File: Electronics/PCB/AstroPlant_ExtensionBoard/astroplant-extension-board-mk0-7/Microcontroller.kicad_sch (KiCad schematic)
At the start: 15 parts, among them IC1 STM32WB55CCU6, J6 629105136821, U1 USBLC6-2SC6

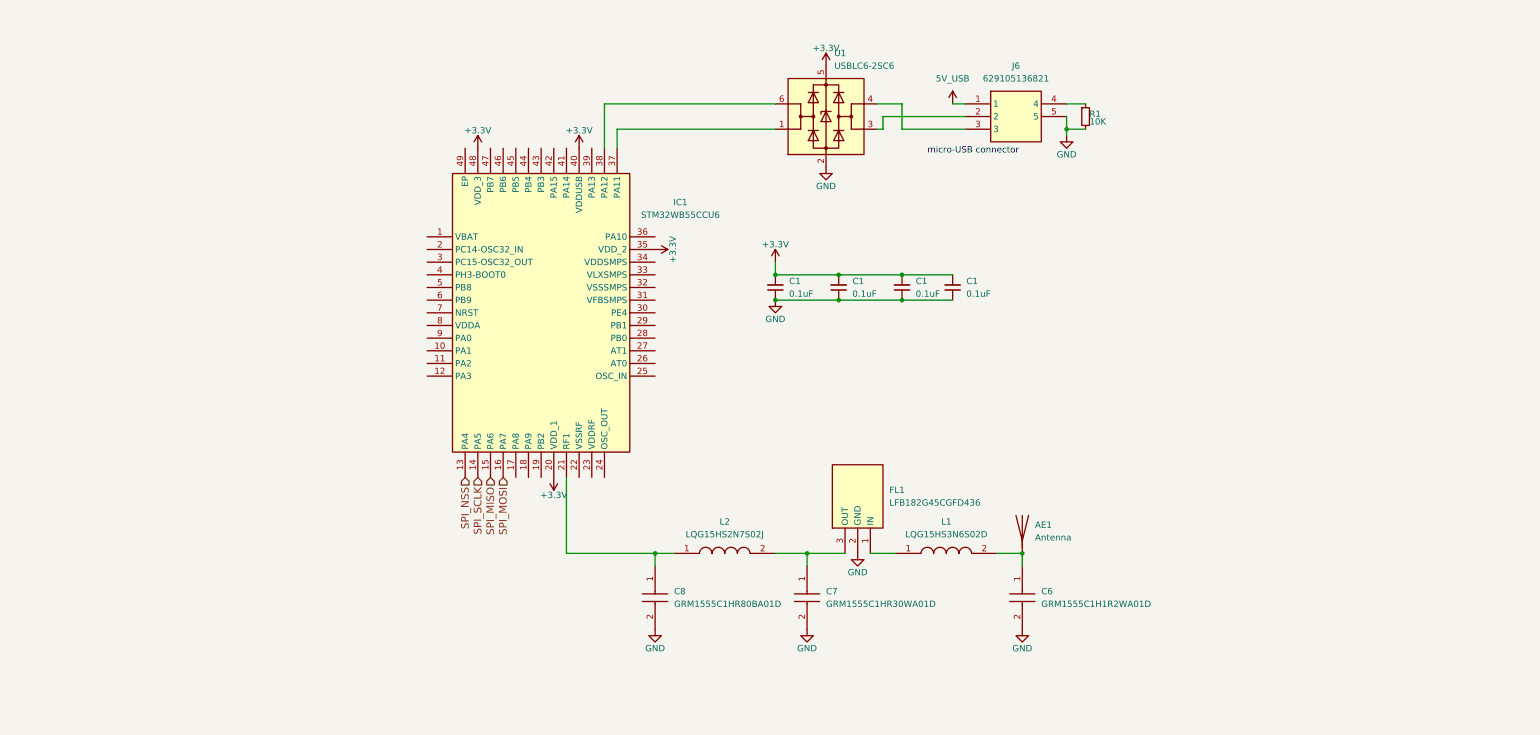
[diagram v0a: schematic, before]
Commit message: Update schematic and change library path
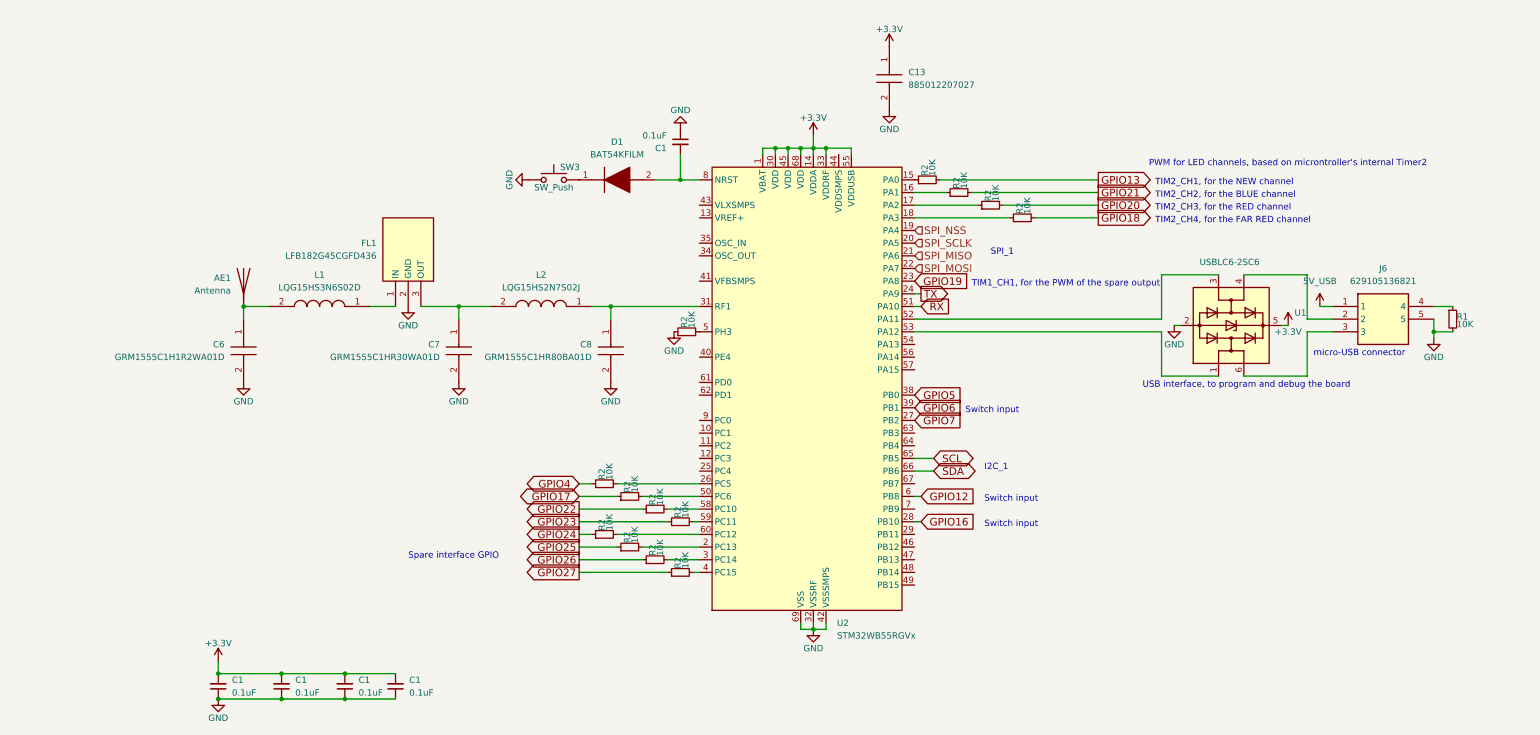
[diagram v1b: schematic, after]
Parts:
- removed IC1: STM32WB55CCU6, QFN50P700X700X60-49N-D, symbol SamacSys_Parts:STM32WB55CCU6
- added C1: 0.1uF, Capacitor_SMD:C_0805_2012Metric, symbol Device:C_Small
- added C13: 885012207027, CAPC2012X90N, symbol SamacSys_Parts:885012207027
- added D1: BAT54KFILM, SODFL1608X70N, symbol SamacSys_Parts:BAT54KFILM
- added R2 (x13): 10K, Resistor_SMD:R_0805_2012Metric, symbol Device:R_Small
- added SW3: SW_Push, Button_Switch_THT:SW_PUSH_6mm, symbol Astroplant_VFR-rescue:SW_Push-Astroplant_VFR-rescue-Astroplant_VFR-rescue
- added U2: STM32WB55RGVx, Package_DFN_QFN:QFN-68-1EP_8x8mm_P0.4mm_EP6.4x6.4mm, symbol MCU_ST_STM32WB:STM32WB55RGVx
- J6: footprint MICRO-USB(2.0-SMT-TYPE-B) -> SamacSys_Parts:MICRO-USB_2.0-SMT-TYPE-B_
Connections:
- net +3V3: now also C13.1, U2.1 (VBAT), U2.14 (VDDA), U2.30 (VDD), U2.33 (VDDRF), U2.45 (VDD), U2.55 (VDDUSB), U2.68 (VDD)
- net GND: now also C1.1, C13.2, R2.1, SW3.1, U2.32 (VSSRF), U2.42 (VSSSMPS), U2.69 (VSS)
- net SPI_MISO: now also U2.21 (PA6)
- net SPI_MOSI: now also U2.22 (PA7)
- net SPI_NSS: now also U2.19 (PA4)
- net SPI_SCLK: now also U2.20 (PA5)
- net at J6.2: now also U1.4 (I/O2); no longer U1.3 (I/O2)
- net at J6.3: now also U1.6 (I/O1); no longer U1.4 (I/O2)
- net at U1.1 (I/O1): now also U2.53 (PA12)
- net at C8.1, L2.1: now also U2.31 (RF1)
- new net: R2.2, U2.5 (PH3)
- new net: R2.2, U2.60 (PC12)
- new net: R2.2, U2.2 (PC13)
- new net: R2.2, U2.4 (PC15)
- new net: R2.1, U2.15 (PA0)
- new net: R2.2, U2.58 (PC10)
- new net: R2.1, U2.18 (PA3)
- new net: U1.3 (I/O2), U2.52 (PA11)
- new net: D1.1, SW3.2
- new net: R2.1, U2.16 (PA1)
- new net: R2.1, U2.17 (PA2)
- new net: R2.2, U2.26 (PC5)
- new net: R2.2, U2.3 (PC14)
- new net: R2.2, U2.50 (PC6)
- new net: R2.2, U2.59 (PC11)
- new net: C1.2, D1.2, U2.8 (NRST)
- new net GPIO12: U2.6 (PB8)
- new net GPIO13: R2.2
- new net GPIO16: U2.28 (PB10)
- new net GPIO17: R2.1
- new net GPIO18: R2.2
- new net GPIO19: U2.23 (PA8)
- new net GPIO20: R2.2
- new net GPIO21: R2.2
- new net GPIO22: R2.1
- new net GPIO23: R2.1
- new net GPIO24: R2.1
- new net GPIO25: R2.1
- new net GPIO26: R2.1
- new net GPIO27: R2.1
- new net GPIO4: R2.1
- new net GPIO5: U2.38 (PB0)
- new net GPIO6: U2.39 (PB1)
- new net GPIO7: U2.27 (PB2)
- new net RX: U2.51 (PA10)
- new net SCL: U2.65 (PB5)
- new net SDA: U2.66 (PB6)
- new net TX: U2.24 (PA9)
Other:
- note added: "I2C_1"
- note added: "PWM for LED channels, based on microntroller's internal Timer2"
- note added: "SPI_1"
- note added: "Spare interface GPIO"
- note added: "Switch input"
- note added: "TIM1_CH1, for the PWM of the spare output"
- note added: "TIM2_CH1, for the NEW channel"
- note added: "TIM2_CH2, for the BLUE channel"
- note added: "TIM2_CH3, for the RED channel"
- note added: "TIM2_CH4, for the FAR RED channel"
- note added: "USB interface, to program and debug the board"
- moved on the sheet: AE1, C1, C6, C7, C8, FL1, J6, L1, L2, R1, U1

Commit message: Place components on PCB
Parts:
- removed C1 (x5): 0.1uF, Capacitor_SMD:C_0805_2012Metric, symbol Device:C_Small
- removed C13: 885012207027, CAPC2012X90N, symbol SamacSys_Parts:885012207027
- removed R1, R2 (x13): 10K, Resistor_SMD:R_0805_2012Metric, symbol Device:R_Small
- added C10, C11, C12, C14, C5, C9: 100nF, Capacitor_SMD:C_0603_1608Metric, symbol Device:C_Small
- added C13: 100pF, Capacitor_SMD:C_0603_1608Metric, symbol Device:C_Small
- added R12, R24: 10k, Resistor_SMD:R_0603_1608Metric, symbol Device:R_Small
- added R13, R14, R15, R16, R17, R18, R19, R20, R21, R22, R23, R6: 1k, Resistor_SMD:R_0603_1608Metric, symbol Device:R_Small
- C6, C7, C8: footprint CAPC1005X55N -> SamacSys_Parts:CAPC1005X55N
- D1: footprint SODFL1608X70N -> SamacSys_Parts:SODFL1608X70N
- FL1: footprint LFB182G45CGFD436 -> SamacSys_Parts:LFB182G45CGFD436
- L1, L2: footprint LQG15WH0N7B02D -> SamacSys_Parts:LQG15WH0N7B02D
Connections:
- net +3V3: now also C10.1, C11.1, C13.1, C14.1, C5.1, C9.1; no longer U2.1 (VBAT)
- net GND: now also C10.2, C11.2, C12.1, C13.2, C14.2, C5.2, C9.2, R12.1, R24.1
- net GPIO13: now also R15.2
- net GPIO17: now also R21.1
- net GPIO18: now also R6.2
- net GPIO20: now also R13.2
- net GPIO21: now also R14.2
- net GPIO22: now also R22.1
- net GPIO23: now also R23.1
- net GPIO24: now also R19.1
- net GPIO25: now also R18.1
- net GPIO26: now also R17.1
- net GPIO27: now also R16.1
- net GPIO4: now also R20.1
- net at J6.4: now also R12.2
- net at U2.5 (PH3): now also R24.2
- net at U2.60 (PC12): now also R19.2
- net at U2.2 (PC13): now also R18.2
- net at U2.4 (PC15): now also R16.2
- net at U2.15 (PA0): now also R15.1
- net at U2.58 (PC10): now also R22.2
- net at U2.18 (PA3): now also R6.1
- net at U2.16 (PA1): now also R14.1
- net at U2.17 (PA2): now also R13.1
- net at U2.26 (PC5): now also R20.2
- net at U2.3 (PC14): now also R17.2
- net at U2.50 (PC6): now also R21.2
- net at U2.59 (PC11): now also R23.2
- net at D1.2, U2.8 (NRST): now also C12.2

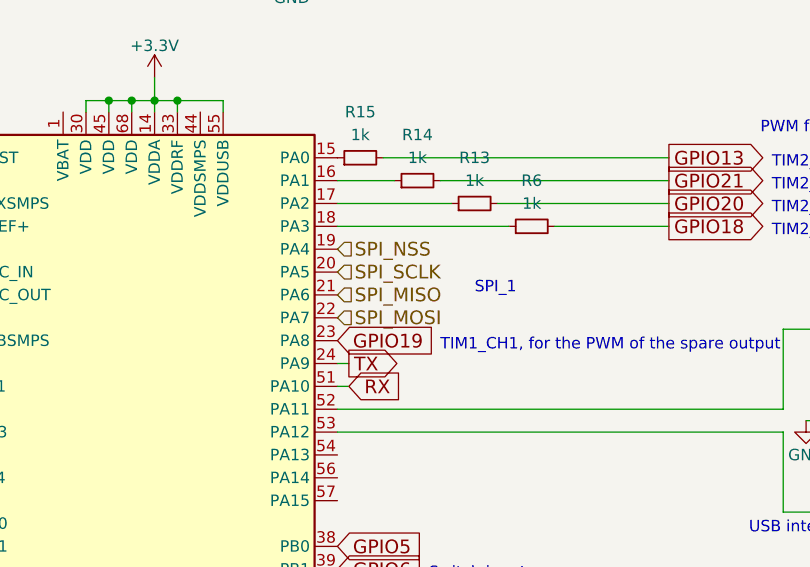
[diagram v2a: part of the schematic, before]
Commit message: Add route to PCB
Not the final version of the PCB, missing components for the antenna and also non-component things like the astroplant logo, the version and placement of the component designators.
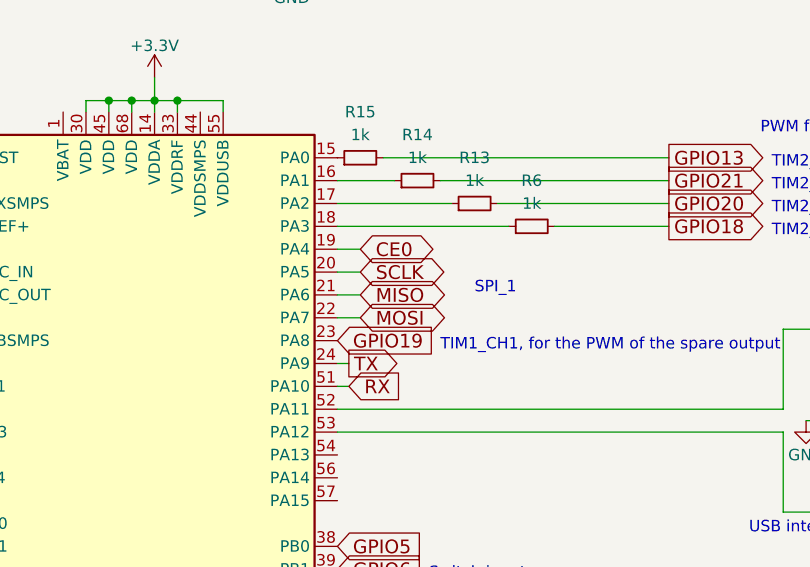
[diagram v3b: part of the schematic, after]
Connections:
- net SPI_MISO renamed MISO
- net SPI_MOSI renamed MOSI
- net SPI_NSS renamed CE0
- net SPI_SCLK renamed SCLK
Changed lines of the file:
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@@
+    (stroke (width 0) (type default))
+  )
+  (wire (pts (xy 175.26 63.5) (xy 172.72 63.5))
     (stroke (width 0) (type default))
   )
@@
     (stroke (width 0) (type default))
   )
+  (wire (pts (xy 175.26 60.96) (xy 172.72 60.96))
+    (stroke (width 0) (type default))
+  )
   (wire (pts (xy 128.27 129.54) (xy 129.54 129.54))
     (stroke (width 0) (type default))
@@
     (stroke (width 0) (type default))
   )
+  (wire (pts (xy 175.26 68.58) (xy 172.72 68.58))
+    (stroke (width 0) (type default))
+  )
   (wire (pts (xy 125.73 50.8) (xy 125.73 45.72))
     (stroke (width 0) (type default))
@@
   )
   (wire (pts (xy 149.86 139.7) (xy 149.86 140.97))
+    (stroke (width 0) (type default))
+  )
+  (wire (pts (xy 175.26 66.04) (xy 172.72 66.04))
     (stroke (width 0) (type default))
   )
@@
     )
   )
+  (global_label "CE0" (shape bidirectional) (at 175.26 60.96 0)
+    (effects (font (size 1.524 1.524)) (justify left))
+    (property "Intersheetrefs" "${INTERSHEET_REFS}" (at 175.26 60.96 0)
+      (effects (font (size 1.27 1.27)) hide)
+    )
+  )
   (global_label "SDA" (shape bidirectional) (at 176.53 109.22 0)
     (effects (font (size 1.524 1.524)) (justify left))
     (property "Intersheetrefs" "${INTERSHEET_REFS}" (at 176.53 109.22 0)
+      (effects (font (size 1.27 1.27)) hide)
+    )
+  )
+  (global_label "SCLK" (shape bidirectional) (at 175.26 63.5 0)
+    (effects (font (size 1.524 1.524)) (justify left))
+    (property "Intersheetrefs" "${INTERSHEET_REFS}" (at 175.26 63.5 0)
       (effects (font (size 1.27 1.27)) hide)
     )
@@
     )
   )
+  (global_label "MISO" (shape bidirectional) (at 175.26 66.04 0)
+    (effects (font (size 1.524 1.524)) (justify left))
+    (property "Intersheetrefs" "${INTERSHEET_REFS}" (at 175.26 66.04 0)
+      (effects (font (size 1.27 1.27)) hide)
+    )
+  )
   (global_label "GPIO13" (shape output) (at 209.55 50.8 0)
     (effects (font (size 1.524 1.524)) (justify left))
@@
     (effects (font (size 1.524 1.524)) (justify right))
     (property "Intersheetrefs" "${INTERSHEET_REFS}" (at 105.41 129.54 0)
+      (effects (font (size 1.27 1.27)) hide)
+    )
+  )
+  (global_label "MOSI" (shape bidirectional) (at 175.26 68.58 0)
+    (effects (font (size 1.524 1.524)) (justify left))
+    (property "Intersheetrefs" "${INTERSHEET_REFS}" (at 175.26 68.58 0)
       (effects (font (size 1.27 1.27)) hide)
     )
@@
     )
   )
-  (hierarchical_label "SPI_NSS" (shape input) (at 172.72 60.96 0) (fields_autoplaced)
-    (effects (font (size 1.524 1.524)) (justify left))
-  )
-  (hierarchical_label "SPI_SCLK" (shape input) (at 172.72 63.5 0) (fields_autoplaced)
-    (effects (font (size 1.524 1.524)) (justify left))
-  )
-  (hierarchical_label "SPI_MISO" (shape input) (at 172.72 66.04 0) (fields_autoplaced)
-    (effects (font (size 1.524 1.524)) (justify left))
-  )
-  (hierarchical_label "SPI_MOSI" (shape input) (at 172.72 68.58 0) (fields_autoplaced)
-    (effects (font (size 1.524 1.524)) (justify left))
-  )
   (symbol (lib_id "Device:R_Small") (at 125.73 129.54 90) (unit 1)

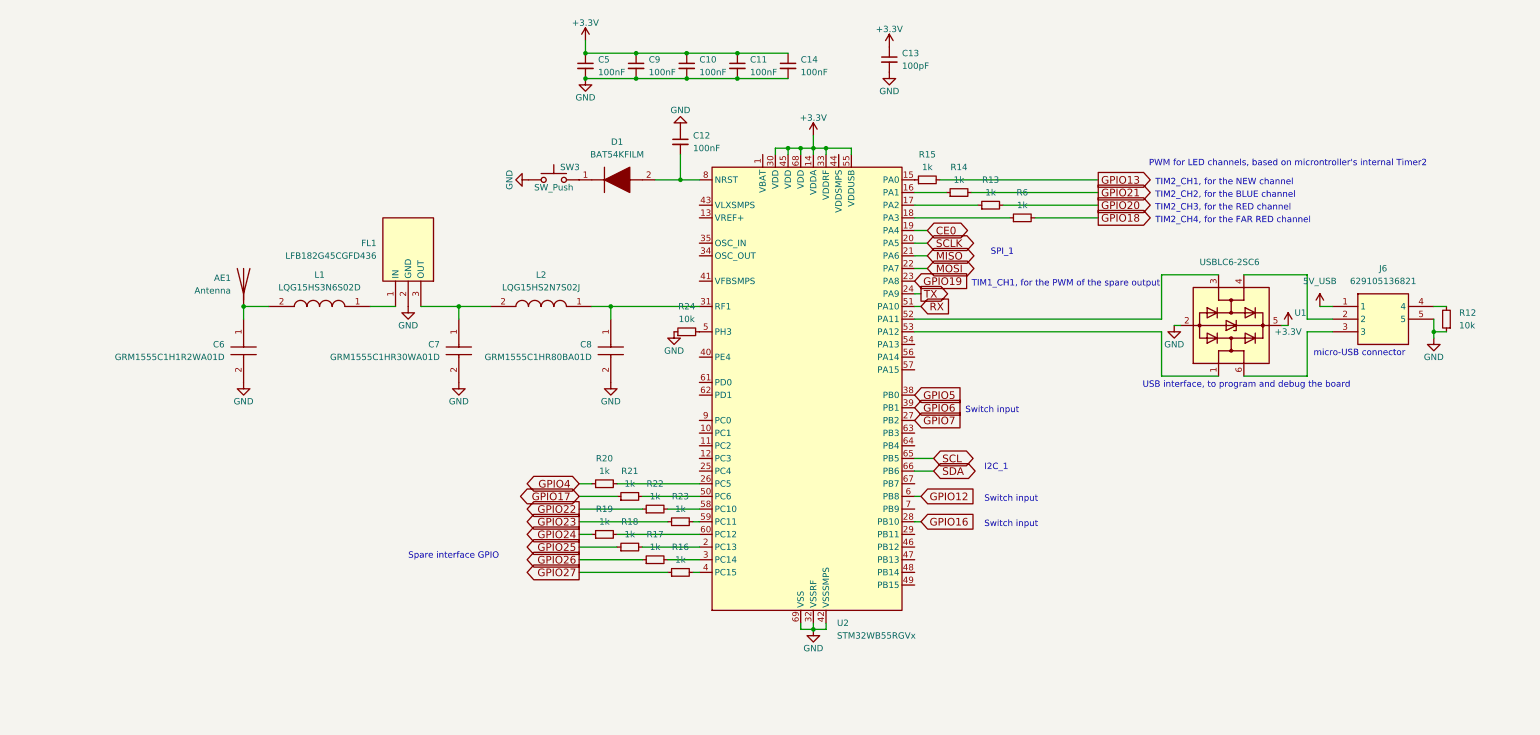
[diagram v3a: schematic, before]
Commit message: Completed version of the project
Generate outputs (BOM, Drill, Pkp, Gerber)
Added connectors descritption (like "I2C 3.3V" dor the corresponding connector)
Added a connector to an external antenna
Changed routing
Changed component placement
Added a script to generate a usable BOM
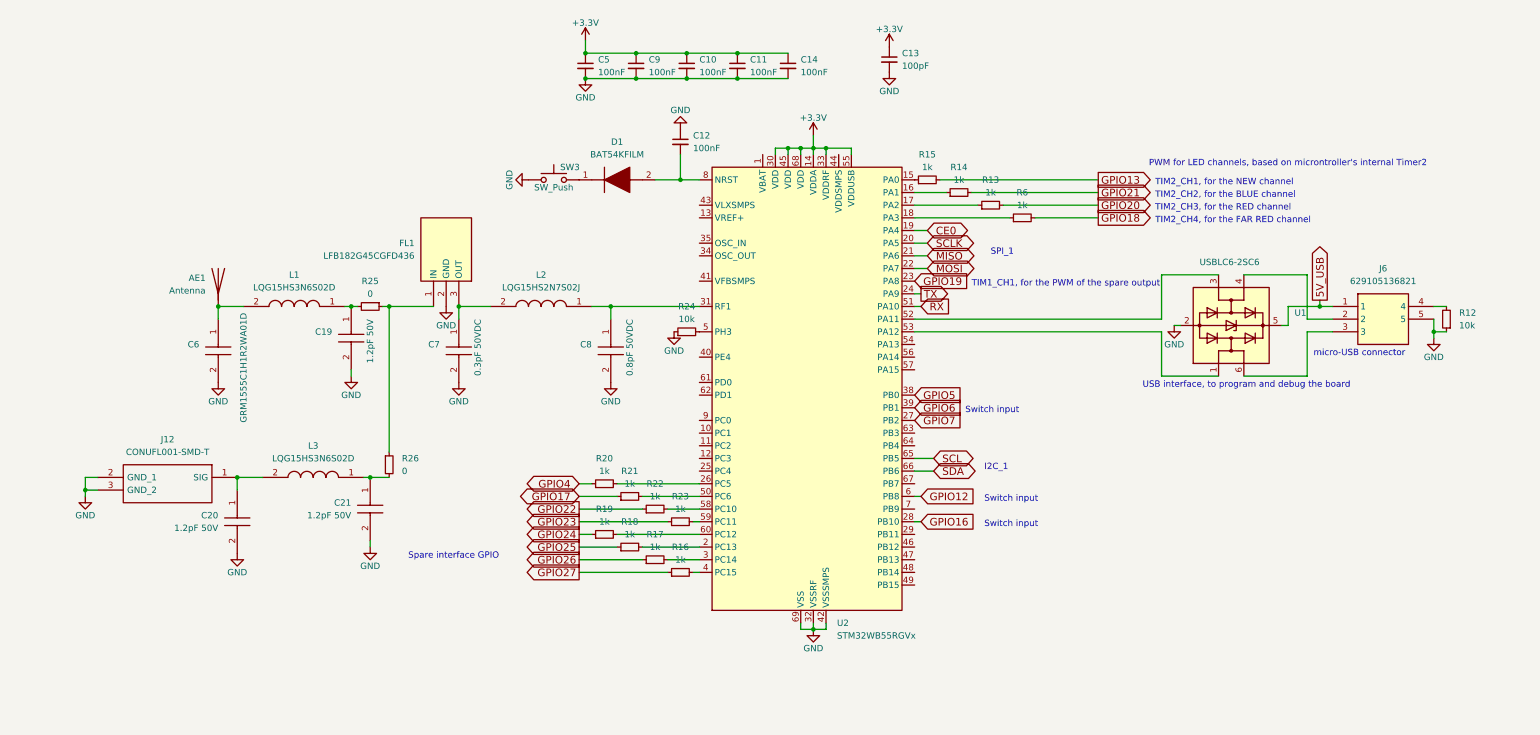
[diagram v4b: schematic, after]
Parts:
- added C19, C20, C21: 1.2pF 50V, SamacSys_Parts:CAPC1005X55N, symbol SamacSys_Parts:GRM1555C1H1R2WA01D
- added J12: CONUFL001-SMD-T, CONUFL001-SMD, symbol SamacSys_Parts:CONUFL001-SMD-T
- added L3: LQG15HS3N6S02D, SamacSys_Parts:LQG15WH0N7B02D, symbol SamacSys_Parts:LQG15HS3N6S02D
- added R25, R26: 0, Resistor_SMD:R_0603_1608Metric, symbol Device:R_Small
- AE1: footprint (none) -> RF_Antenna:Texas_SWRA117D_2.4GHz_Left
- C6: MPN (none) -> GRM1555C1H1R2WA01D
- C7: value GRM1555C1HR30WA01D -> 0.3pF 50VDC; Arrow Part Number GRM1555C1HR30WA01D -> (none); MPN (none) -> GRM1555C1HR30WA01D
- C8: value GRM1555C1HR80BA01D -> 0.8pF 50VDC; Arrow Part Number GRM1555C1HR80BA01D -> (none); MPN (none) -> GRM1555C1HR80BA01D
- D1: Arrow Part Number BAT54KFILM -> (none); MPN (none) -> BAT54KFILM
- FL1: MPN (none) -> LFB182G45CGFD436; Manufacturer_Part_Number LFB182G45CGFD436 -> (none)
- J6: MPN (none) -> 629105136821; Manufacturer_Part_Number 629105136821 -> (none)
- L1: MPN (none) -> LQG15HS3N6S02D
- L2: MPN (none) -> LQG15HS2N7S02J
- U1: MPN (none) -> USBLC6-2SC6
- U2: MPN (none) -> STM32WB55RGVx
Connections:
- net +3V3: no longer J6.1, U1.5 (VBUS)
- net GND: now also C19.2, C20.2, C21.2, J12.2 (GND_1), J12.3 (GND_2)
- net at FL1.1 (IN): now also R25.1, R26.1; no longer L1.1
- new net: C20.1, J12.1 (SIG), L3.2
- new net: C21.1, L3.1, R26.2
- new net: C19.1, L1.1, R25.2
- new net 5V_USB: J6.1, U1.5 (VBUS)
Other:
- moved on the sheet: AE1, C6, FL1, L1
